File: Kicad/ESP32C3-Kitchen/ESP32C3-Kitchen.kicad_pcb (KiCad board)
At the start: 2 copper layers, 42 parts, among them J1 Sense, J2 Main AC, J3 Main AC, J4 Main AC, J5 Main AC, Q1 BTA24-800B, Q2 BTA24-800B, Q3 BTA24-800B, SW1 Element 1, SW2 Element 2, SW3 Element 3, U1 MOC3041M, U2 MOC3041M, U3 MOC3041M, U5 HLK-5M05

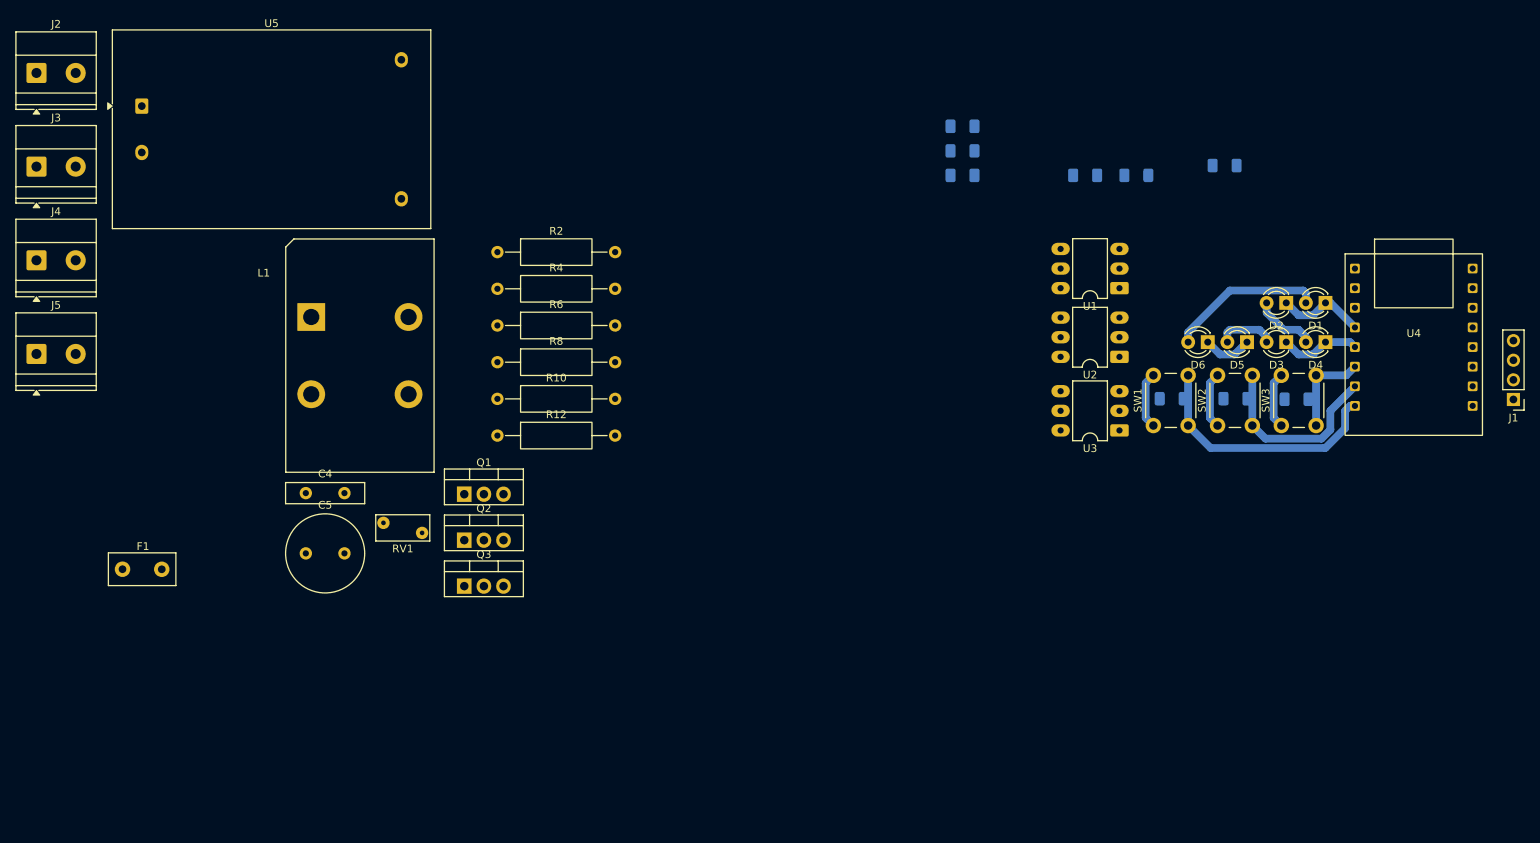
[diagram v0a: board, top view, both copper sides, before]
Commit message: Kicad: Finish one layer version schematic and PCB
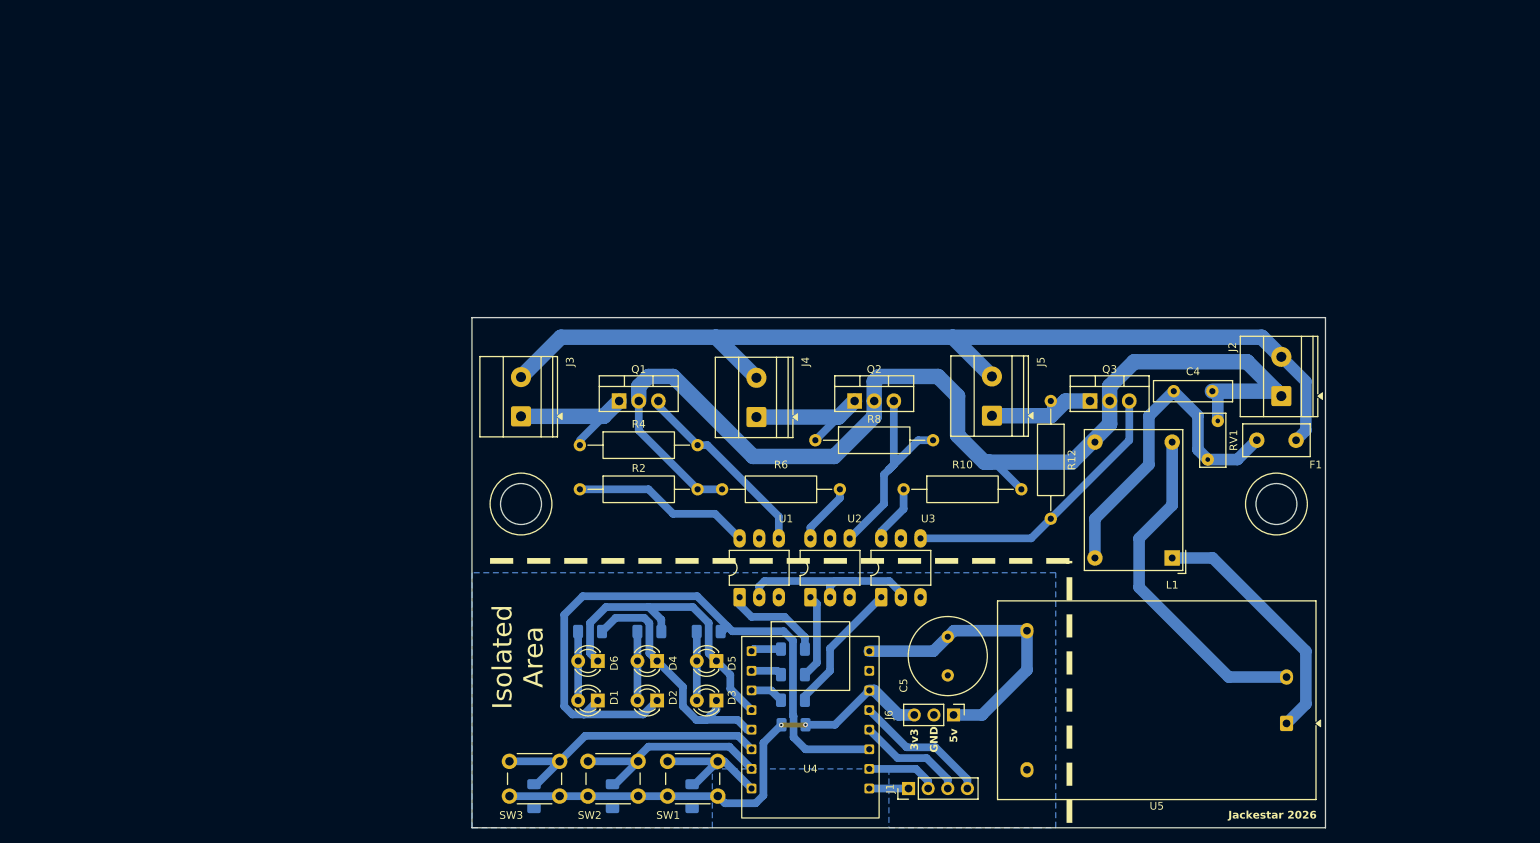
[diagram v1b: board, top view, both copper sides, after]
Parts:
- added J6: Voltage Output, Connector_PinHeader_2.54mm:PinHeader_1x03_P2.54mm_Vertical, F.Cu at (153.8, 116.8)
- added REF**: MountingHole_5.3mm_M5, MountingHole:MountingHole_5.3mm_M5, F.Cu at (97.8, 89.5)
- added REF**: MountingHole_5.3mm_M5, MountingHole:MountingHole_5.3mm_M5, F.Cu at (195.6, 89.5)
- added REF**: R_1206_3216Metric_Pad1.30x1.75mm_HandSolder, Resistor_SMD:R_1206_3216Metric_Pad1.30x1.75mm_HandSolder, B.Cu at (133.1, 118.1)
- L1: footprint Inductor_THT:L_CommonMode_PulseElectronics_PH9455x105NL_1 -> Inductor_THT:Choke_Schaffner_RN212-04-12.5x18.0mm
- moved U5 168.4 mm to (196.9, 117.9), turned to 180 degrees
- moved J2 166.5 mm to (196.2, 75.6), turned to 90 degrees
- moved F1 152.8 mm to (198.1, 81.3), turned to 180 degrees
- moved J5 123.9 mm to (158.8, 78.1), turned to 90 degrees
- moved L1 115.7 mm to (182.1, 96.5), turned to 180 degrees
- moved C4 113.1 mm to (182.3, 74.9)
- moved R18 111.3 mm to (99.5, 127.4), turned to 90 degrees
- moved D1 107.4 mm to (107.7, 115.0)
- moved RV1 107.0 mm to (186.7, 83.8), turned to 90 degrees
- moved SW3 105.0 mm to (102.8, 127.3), turned to 180 degrees
- moved D2 96.3 mm to (115.4, 115.0)
- moved D4 95.9 mm to (115.4, 109.9)
- moved R15 95.8 mm to (114.4, 106.0)
- moved R17 95.7 mm to (109.6, 127.4), turned to 90 degrees
- moved J4 95.4 mm to (128.3, 78.3), turned to 90 degrees
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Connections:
- C4 pad 2: LINE B -> LINE A
- F1 pad 1: LINE A -> LINE B
- L1 pad 1: Net-(C4-Pad1) -> Net-(U5-AC/L)
- L1 pad 2: Net-(U5-AC/L) -> Net-(C4-Pad1)
- L1 pad 3: LINE B -> Net-(U5-AC/N)
- L1 pad 4: Net-(U5-AC/N) -> LINE A
- RV1 pad 2: LINE B -> LINE A
- U4 pad 14: CHP3 -> CHP1
- U4 pad 4: CHP1 -> CHP3
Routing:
- net LINE A: track 0.00 -> 151.2 mm
- net LINE B: track 0.00 -> 128.9 mm
- net CHP1: track 11.5 -> 84.7 mm
- net Net-(U5-AC/N): track 0.00 -> 44.5 mm
- net Net-(C4-Pad1): track 0.00 -> 43.8 mm
- net +3V3: track 22.0 -> 64.2 mm, vias 0 -> 2
- net +5V: track 0.00 -> 38.5 mm
- net Net-(Q3-G): track 0.00 -> 37.4 mm
- net CHP3: track 6.41 -> 39.8 mm
- net Net-(U5-AC/L): track 0.00 -> 32.7 mm
- net Net-(Q2-G): track 0.00 -> 27.4 mm
- net H1_B: track 12.0 -> 37.6 mm
- net GNDD: track 0.00 -> 25.5 mm
- net Net-(Q1-G): track 0.00 -> 25.0 mm
- net CHP2: track 10.5 -> 34.2 mm
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- added copper zone on B.Cu, net GNDD
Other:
- board outline added: 110.5 x 66 mm
- board text added: "3v3"
- board text added: "5v"
- board text added: "GND"
- board text added: "Isolated Area"
- board text added: "Jackestar 2026"
